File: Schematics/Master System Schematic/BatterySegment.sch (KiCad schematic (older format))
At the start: 148 parts

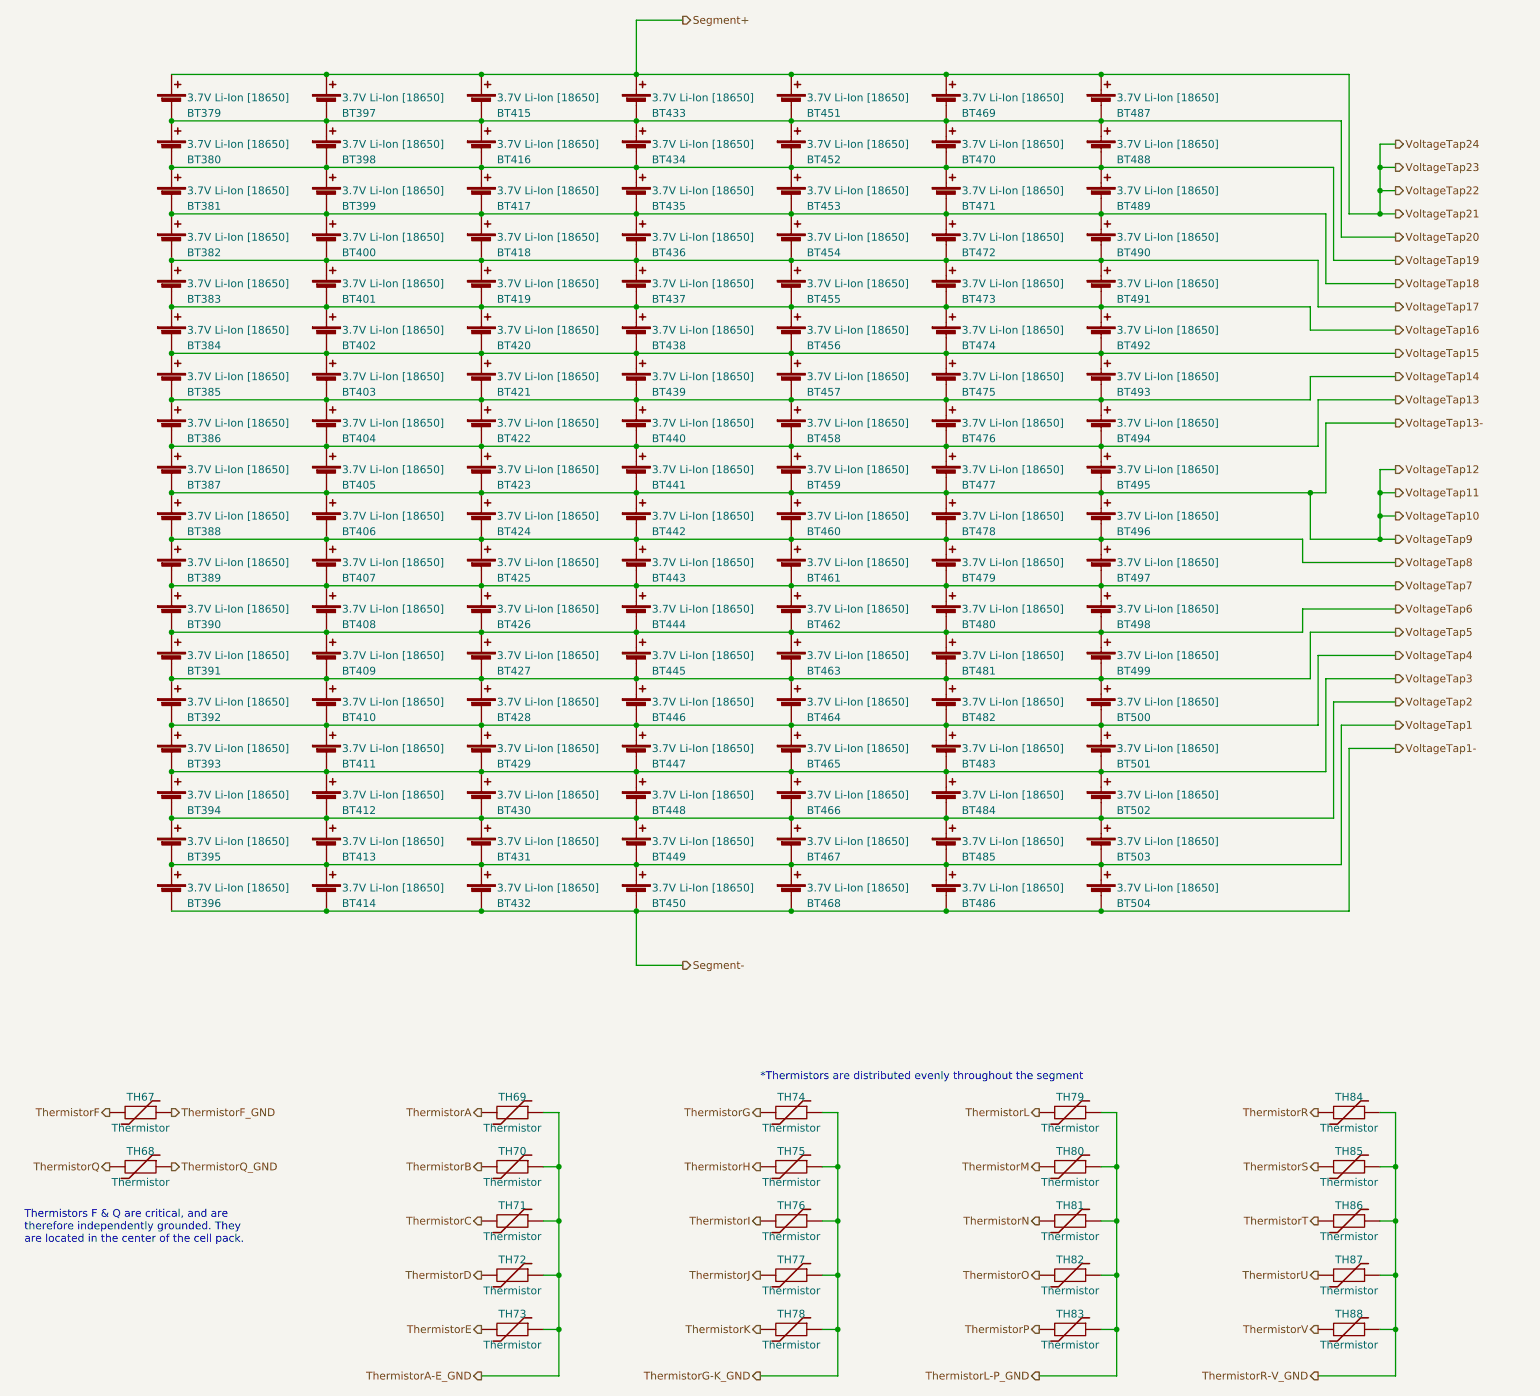
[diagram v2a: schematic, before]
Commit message: FINISHED Voltage tap PCB schem
>reran battery box to fit new schem
>added placeholder thermistor board schem.
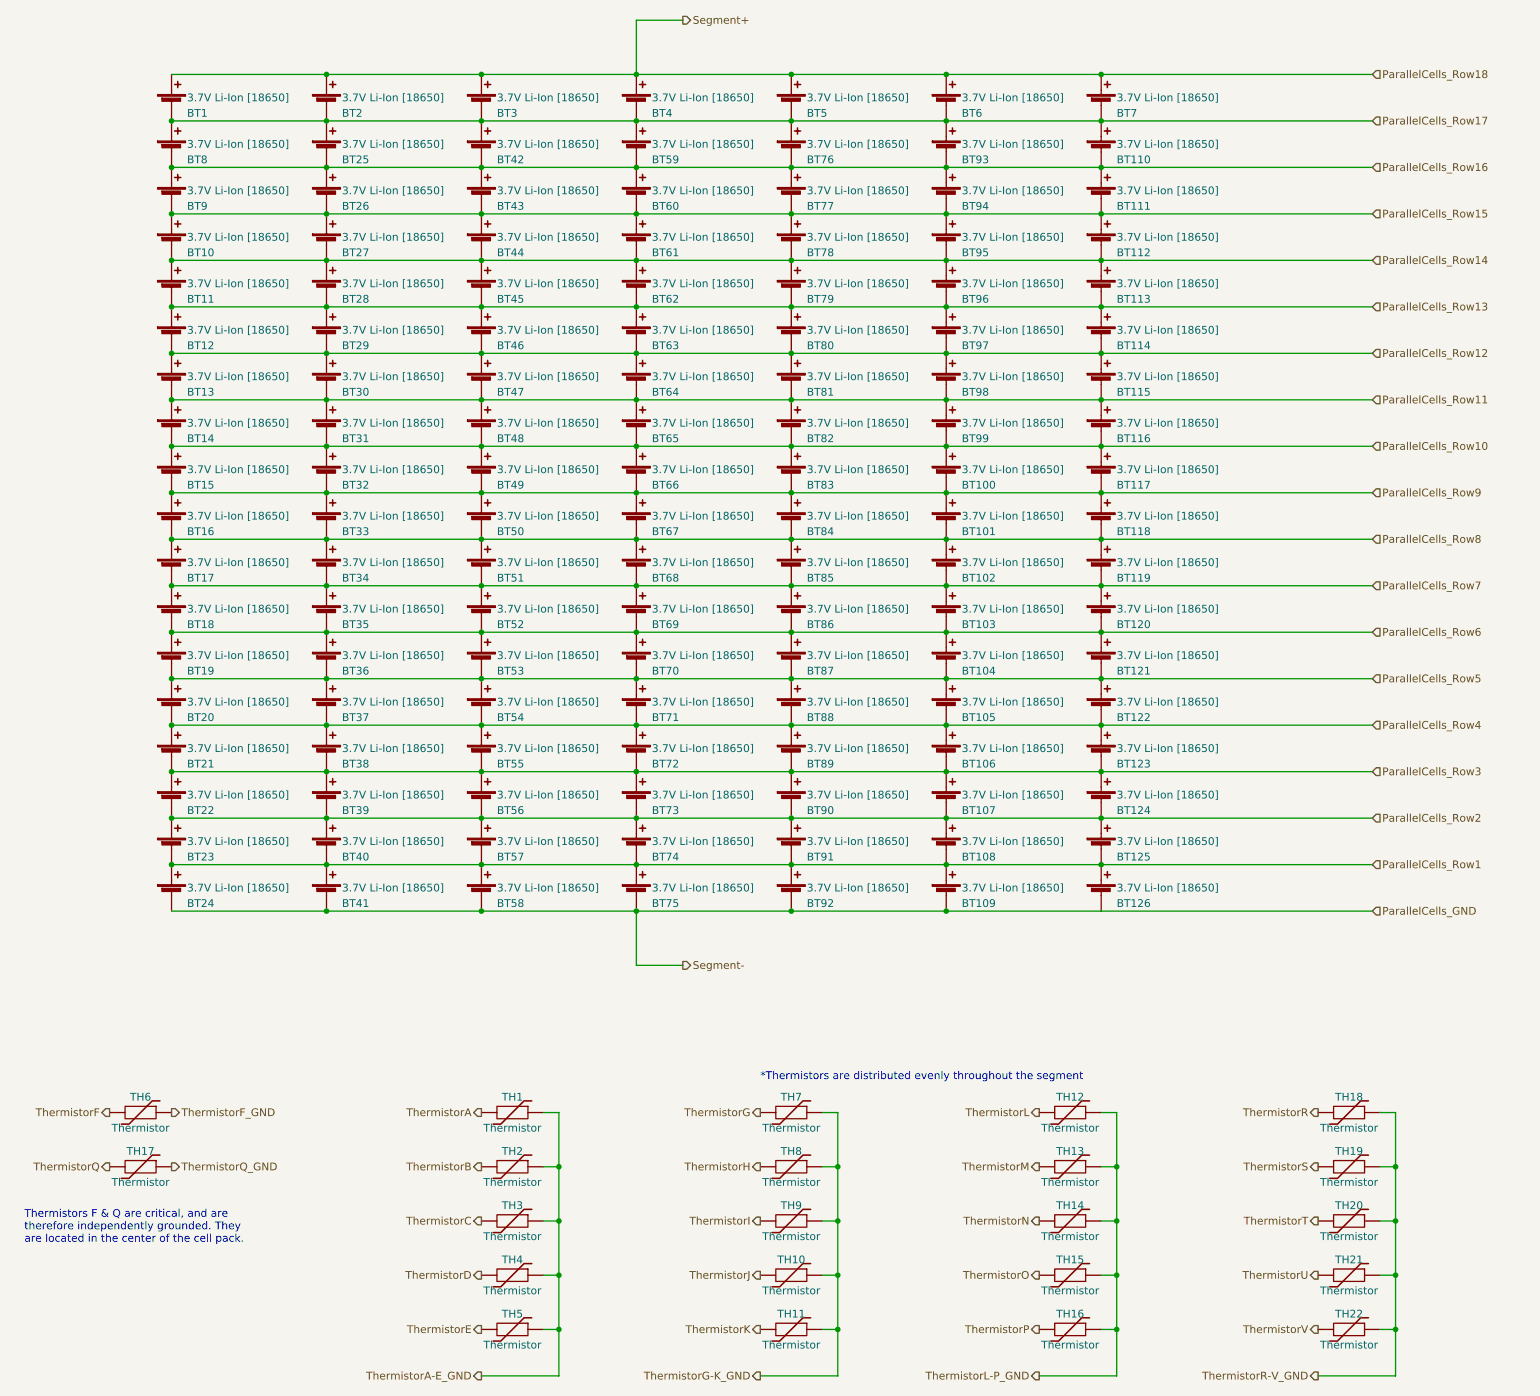
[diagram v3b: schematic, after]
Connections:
- net Segment+ renamed ParallelCells_Row18
- net Segment- renamed ParallelCells_GND
- net VoltageTap1 renamed ParallelCells_Row1
- net VoltageTap10 renamed ParallelCells_Row9
- net VoltageTap13 renamed ParallelCells_Row10
- net VoltageTap14 renamed ParallelCells_Row11
- net VoltageTap15 renamed ParallelCells_Row12
- net VoltageTap16 renamed ParallelCells_Row13
- net VoltageTap17 renamed ParallelCells_Row14
- net VoltageTap18 renamed ParallelCells_Row15
- net VoltageTap19 renamed ParallelCells_Row16
- net VoltageTap2 renamed ParallelCells_Row2
- net VoltageTap20 renamed ParallelCells_Row17
- net VoltageTap3 renamed ParallelCells_Row3
- net VoltageTap4 renamed ParallelCells_Row4
- net VoltageTap5 renamed ParallelCells_Row5
- net VoltageTap6 renamed ParallelCells_Row6
- net VoltageTap7 renamed ParallelCells_Row7
- net VoltageTap8 renamed ParallelCells_Row8
